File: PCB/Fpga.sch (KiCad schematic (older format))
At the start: 14 parts

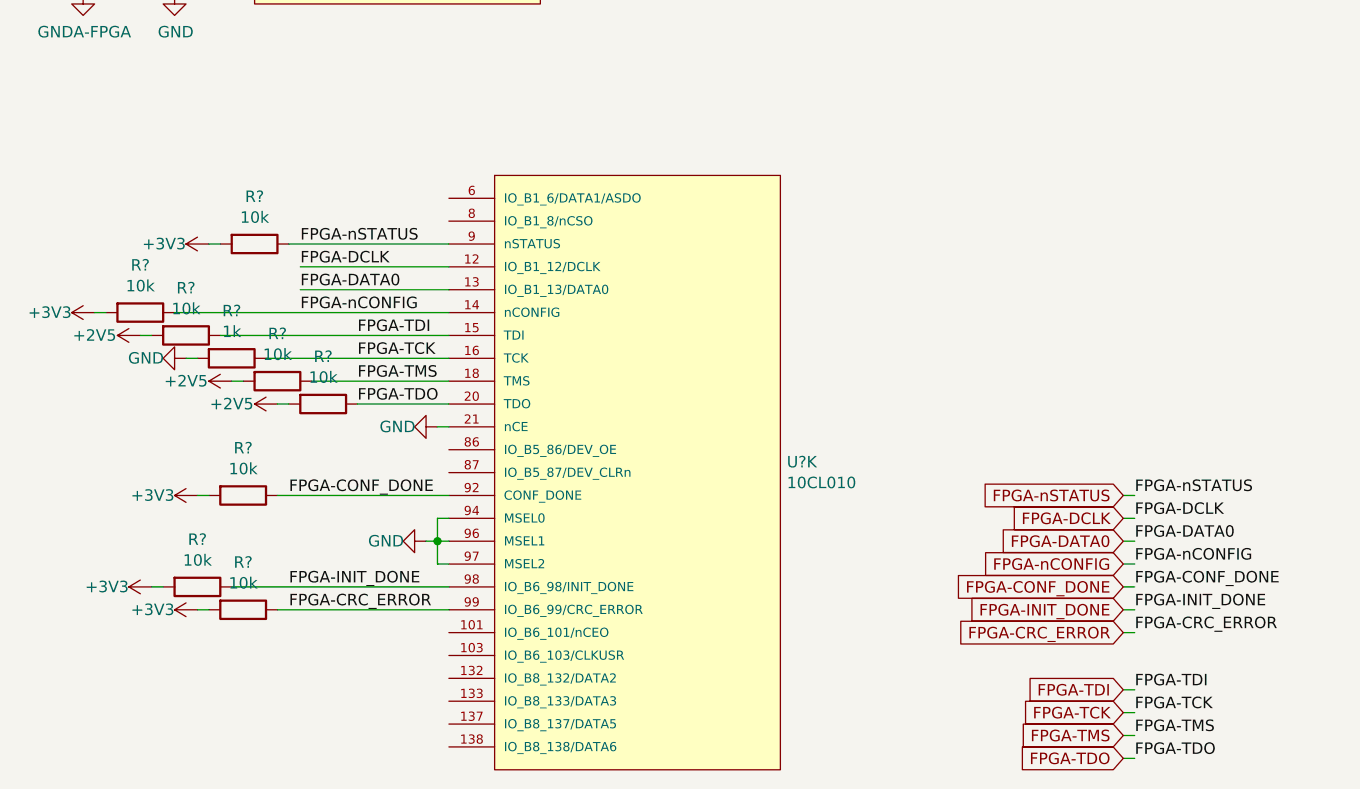
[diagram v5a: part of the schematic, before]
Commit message: Add connections between FPGA and microcontroller
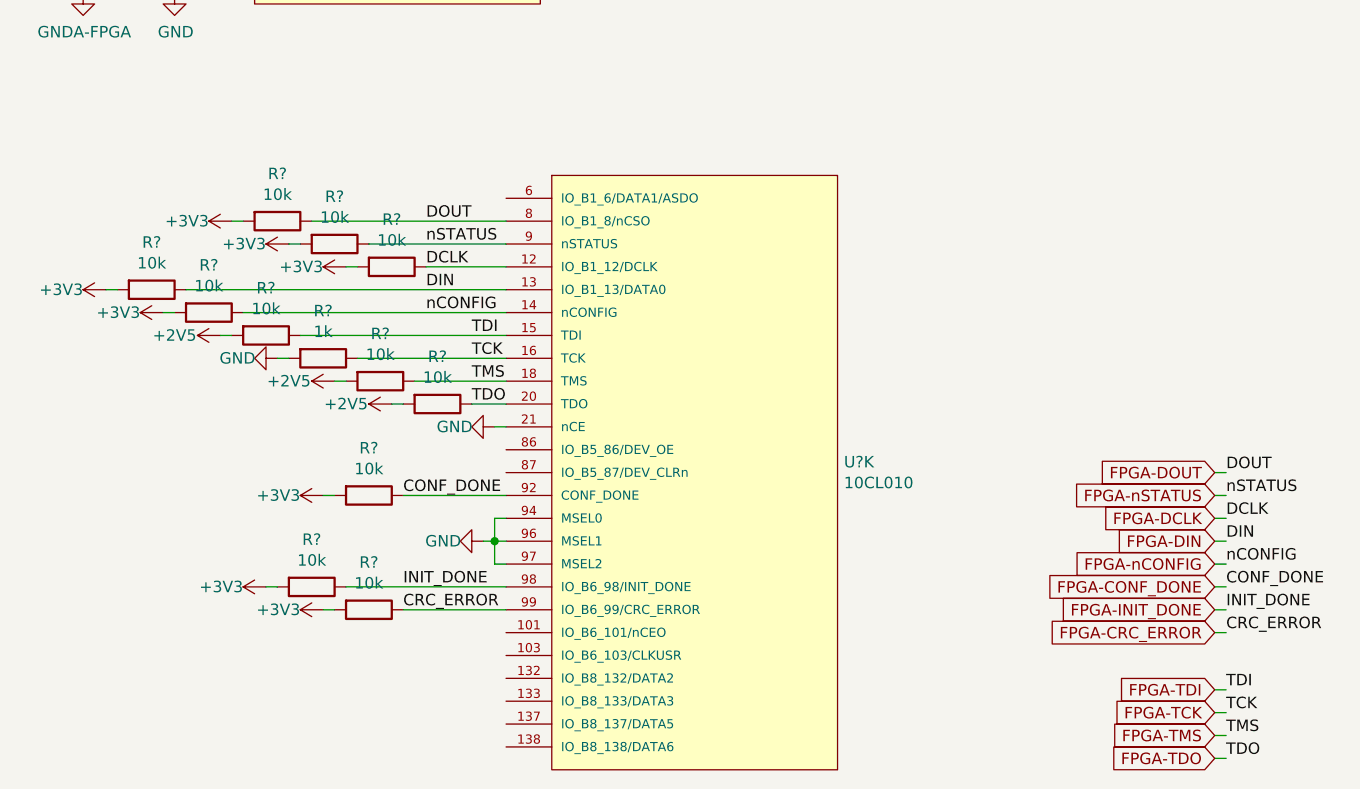
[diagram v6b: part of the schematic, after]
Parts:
- added R? (x3): 10k, Resistors_SMD:R_0603_HandSoldering, symbol Device:R
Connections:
- net +3V3: now also R?.2, R?.2, R?.2
- net FPGA-DCLK: now also R?.1
- net FPGA-DOUT: now reaches U?.8 (IO_B1_8/nCSO)
- net FPGA-DOUT: now also R?.1
- net FPGA-DATA0 renamed FPGA-DIN
- net FPGA-DIN: now also R?.1
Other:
- moved on the sheet: R?, U?K

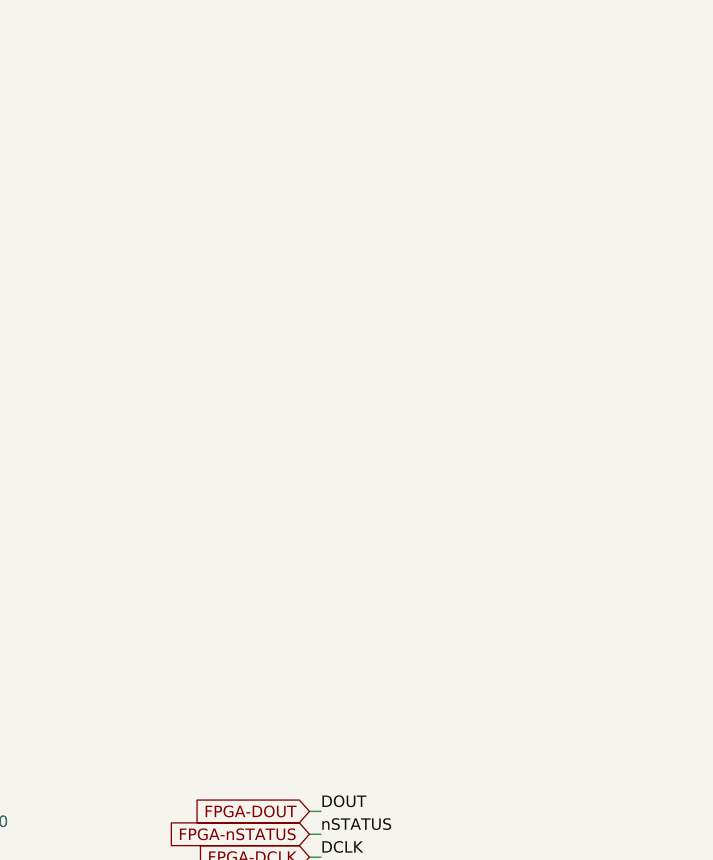
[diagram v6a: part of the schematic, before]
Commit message: Connect push buttons to microcontroller, connect I2C lines, add GPIO links between microcontroller and FPGA
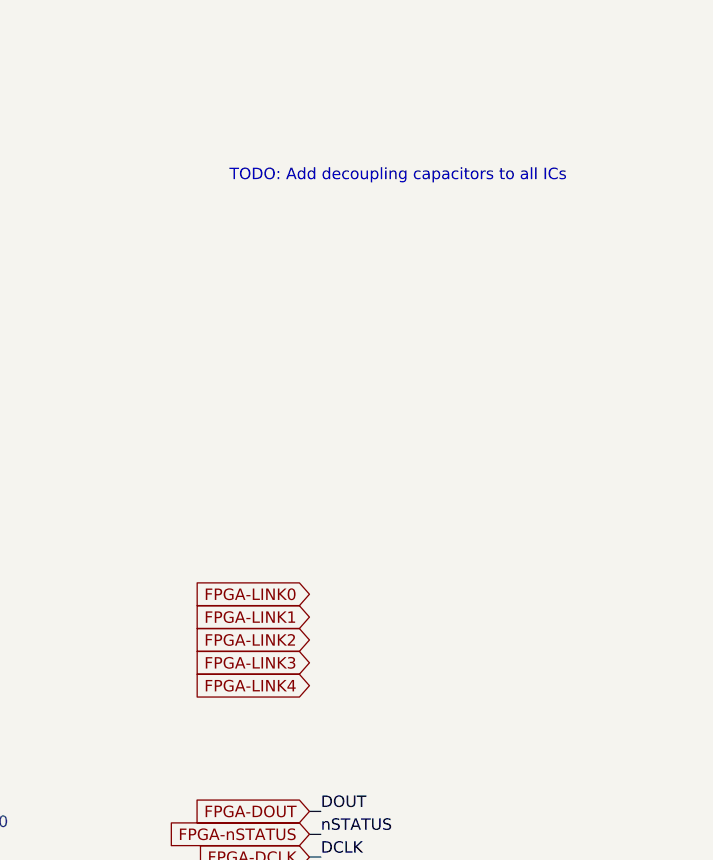
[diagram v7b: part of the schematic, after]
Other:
- note added: "TODO: Add decoupling capacitors to all ICs"
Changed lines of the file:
@@
 Wire Wire Line
 	5750 6350 5800 6350
+Text Notes 5400 3600 0    50   ~ 0
+TODO: Add decoupling capacitors to all ICs
+Text GLabel 5750 5400 0    50   Input ~ 0
+FPGA-LINK0
+Text GLabel 5750 5500 0    50   Input ~ 0
+FPGA-LINK1
+Text GLabel 5750 5600 0    50   Input ~ 0
+FPGA-LINK2
+Text GLabel 5750 5700 0    50   Input ~ 0
+FPGA-LINK3
+Text GLabel 5750 5800 0    50   Input ~ 0
+FPGA-LINK4
 $EndSCHEMATC

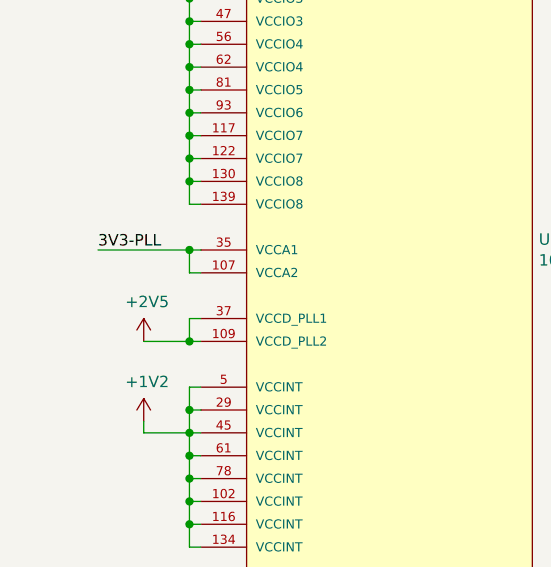
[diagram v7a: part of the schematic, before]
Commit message: Fixed mistake on FPGA power supplies
VCCD_PLL lines were connected to the wrong supply. They need to match the core voltage.
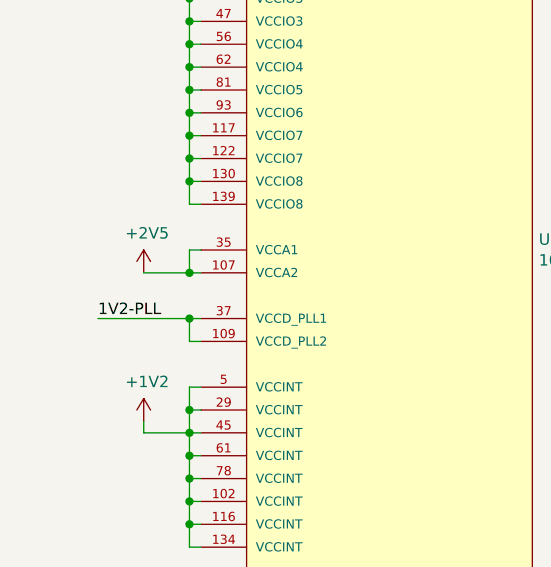
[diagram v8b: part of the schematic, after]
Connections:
- net 3V3-PLL is gone; now on net +2V5: U?.107 (VCCA2), U?.35 (VCCA1)
- net +2V5: no longer U?.109 (VCCD_PLL2), U?.37 (VCCD_PLL1)
- new net 1V2-PLL: U?.109 (VCCD_PLL2), U?.37 (VCCD_PLL1)
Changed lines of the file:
@@
 L power:+2V5 #PWR?
 U 1 1 5DE217EB
-P 1100 2400
-F 0 "#PWR?" H 1100 2250 50  0001 C CNN
-F 1 "+2V5" H 1115 2573 50  0000 C CNN
-F 2 "" H 1100 2400 50  0001 C CNN
-F 3 "" H 1100 2400 50  0001 C CNN
-	1    1100 2400
+P 1100 2100
+F 0 "#PWR?" H 1100 1950 50  0001 C CNN
+F 1 "+2V5" H 1115 2273 50  0000 C CNN
+F 2 "" H 1100 2100 50  0001 C CNN
+F 3 "" H 1100 2100 50  0001 C CNN
+	1    1100 2100
 	1    0    0    -1
 $EndComp
@@
 	1100 900  1300 900
 Wire Wire Line
+	1350 2000 1300 2000
+Wire Wire Line
+	1300 2000 1300 2100
+Wire Wire Line
+	1300 2100 1350 2100
+Wire Wire Line
+	1100 2100 1300 2100
+Connection ~ 1300 2100
+Wire Wire Line
 	1350 2300 1300 2300
+Wire Wire Line
+	1300 2400 1350 2400
+Text Label 900  2300 0    50   ~ 0
+1V2-PLL
 Wire Wire Line
 	1300 2300 1300 2400
 Wire Wire Line
-	1300 2400 1350 2400
-Wire Wire Line
-	1100 2400 1300 2400
-Connection ~ 1300 2400
-Wire Wire Line
-	1350 2000 1300 2000
-Wire Wire Line
-	1300 2100 1350 2100
-Text Label 900  2000 0    50   ~ 0
-3V3-PLL
-Wire Wire Line
-	1300 2000 1300 2100
-Wire Wire Line
-	900  2000 1300 2000
-Connection ~ 1300 2000
+	900  2300 1300 2300
+Connection ~ 1300 2300
 Text GLabel 4550 2000 0    50   Input ~ 0
 DAC-~CS
